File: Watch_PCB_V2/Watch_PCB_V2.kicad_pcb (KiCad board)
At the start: 2 copper layers, 30.5 x 30.5 mm, 14 parts

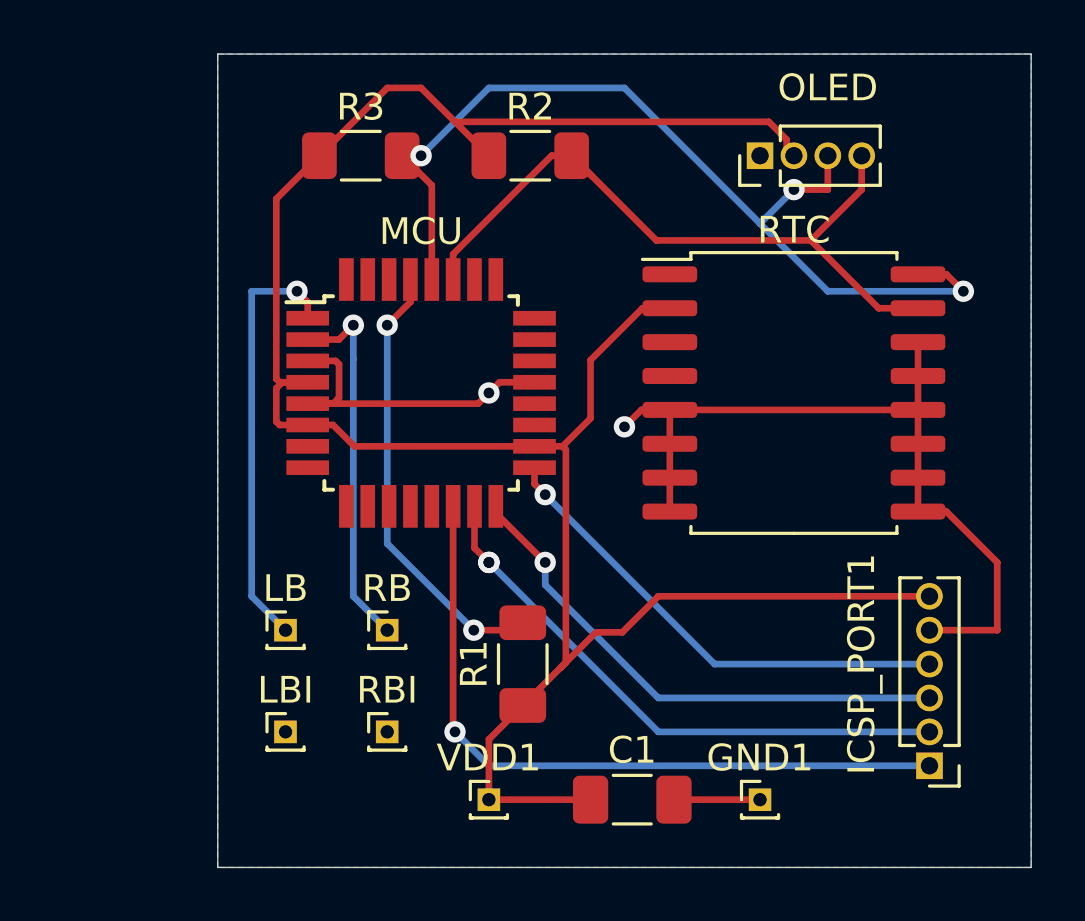
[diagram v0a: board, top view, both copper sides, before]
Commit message: PCB: deep sleep interrupt now attached left button input
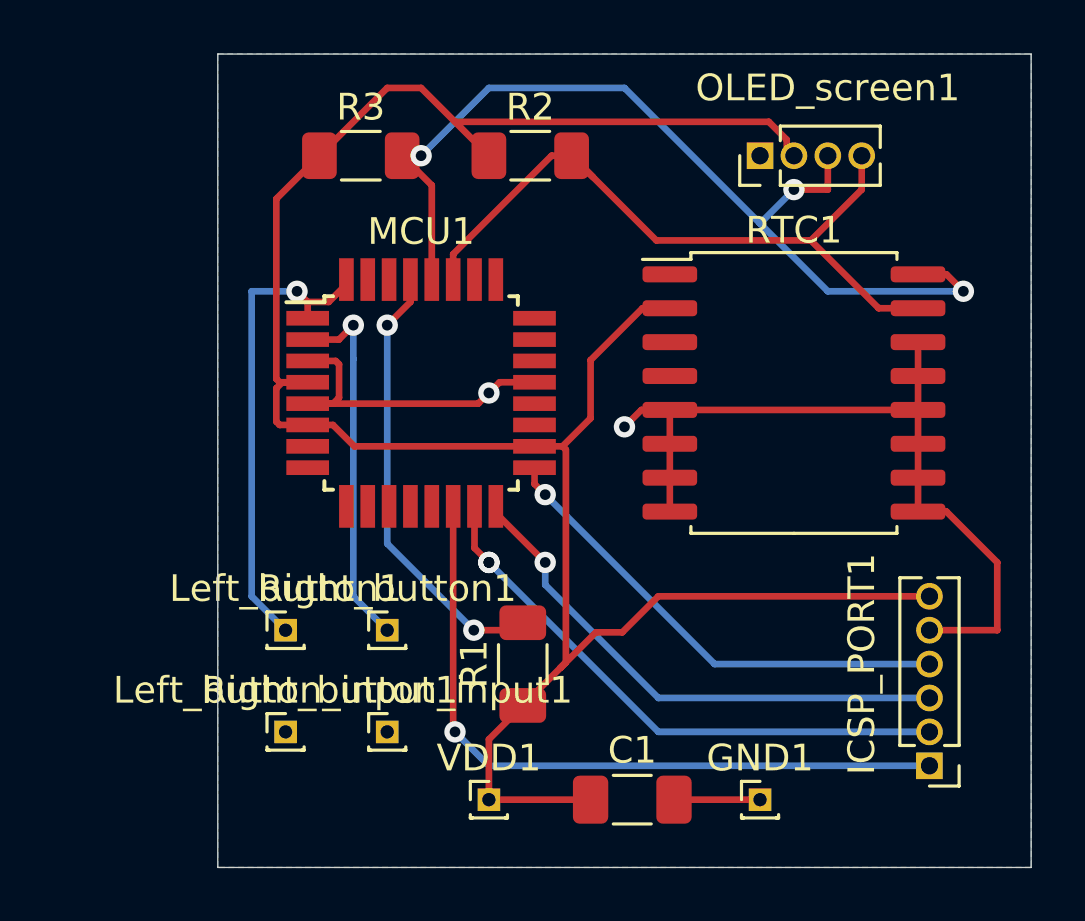
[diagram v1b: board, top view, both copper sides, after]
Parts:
- renumbered LB to Left_button1, LBI to Left_button_input1, MCU to MCU1, OLED to OLED_screen1, RTC to RTC1, RB to Right_button1, RBI to Right_button_input1
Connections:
- MCU1 pad 32: Net-(MCU1-Pad32) -> Net-(Left_button1-Pad1)
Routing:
- net Net-(Left_button1-Pad1): track 16.1 -> 18.0 mm
